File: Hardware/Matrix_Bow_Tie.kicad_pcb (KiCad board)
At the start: 2 copper layers, 17.8 x 13 mm, 2 parts, among them U1 MAX4466

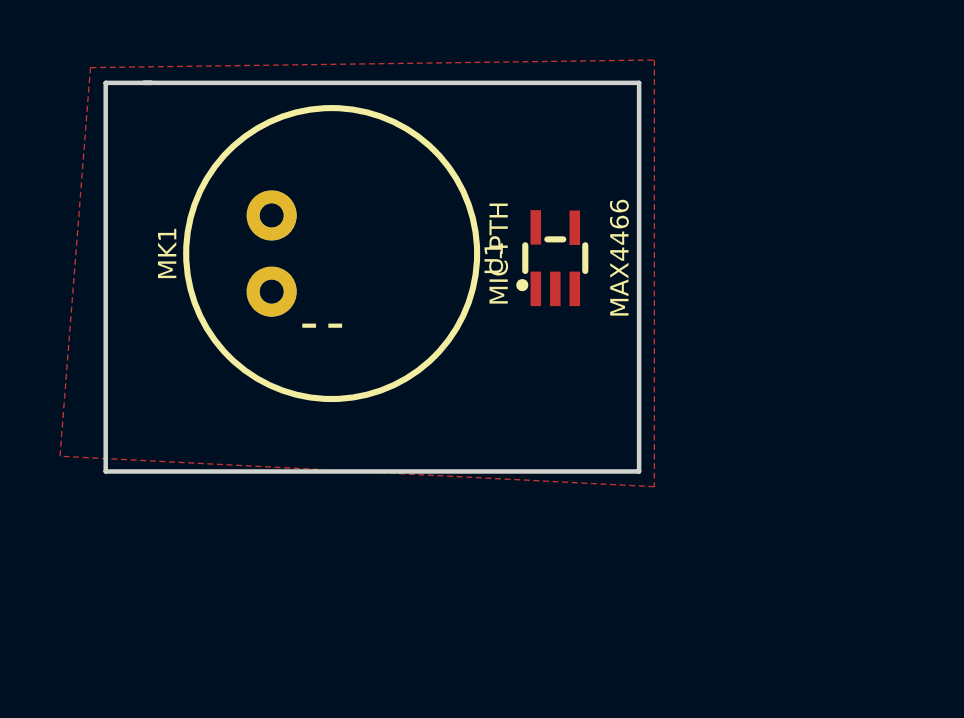
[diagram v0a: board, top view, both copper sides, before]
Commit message: Added trimpot footprint and drew mic amp circuit.
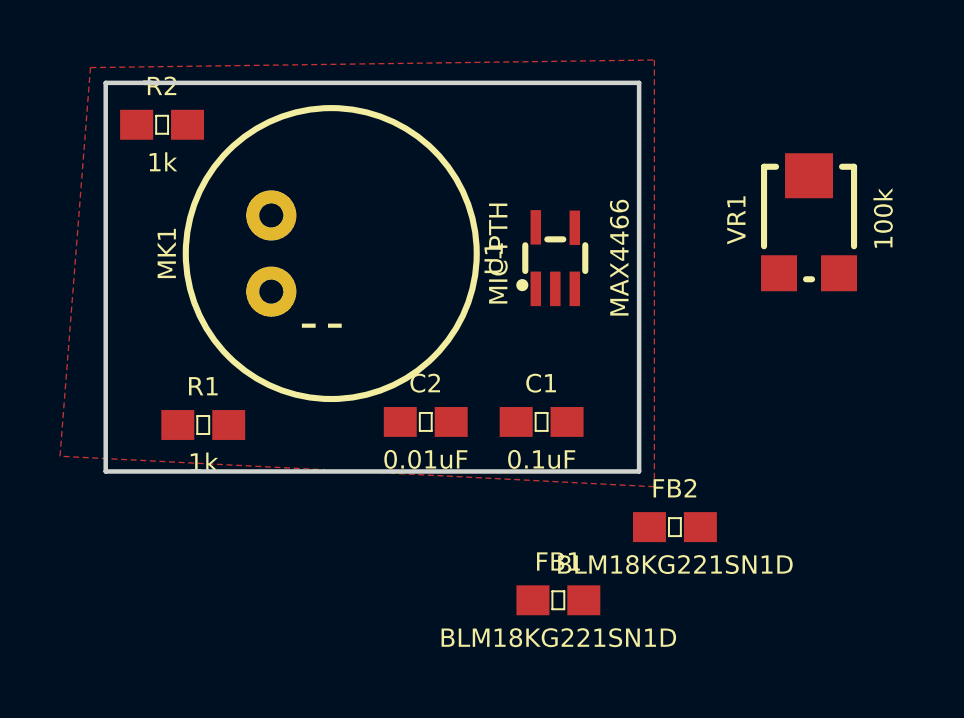
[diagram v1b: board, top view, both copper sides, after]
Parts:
- added C1: 0.1uF, 0603, F.Cu at (155.5, 110.6)
- added C2: 0.01uF, 0603, F.Cu at (151.6, 110.6)
- added FB1: BLM18KG221SN1D, 0603, F.Cu at (156.1, 116.6)
- added FB2: BLM18KG221SN1D, 0603, F.Cu at (159.9, 114.1)
- added R1: 1k, 0603, F.Cu at (144.2, 110.7)
- added R2: 1k, 0603, F.Cu at (142.8, 100.7)
- added VR1: 100k, TC33X, F.Cu at (164.4, 103.9)
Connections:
- net GND renamed AGND
- MK1 pad OUT: Net-(MK1-PadOUT) -> Net-(C2-Pad1)
- U1 pad 1: Net-(MK1-PadOUT) -> Net-(U1-Pad1)

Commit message: Parts mostly laid out
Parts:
- added C3: 10uF, Capacitors:0805, F.Cu at (181.6, 70.5)
- added C4: 100pF, Capacitors:0603, F.Cu at (186.7, 76.8)
- added C5: 0.1uF, Capacitors:0603, F.Cu at (212.1, 120.0)
- added D1: Yellow, LED:LED-0603, B.Cu at (209.5, 102.2)
- added D10: Yellow, LED:LED-0603, B.Cu at (198.1, 135.2)
- added D11: Yellow, LED:LED-0603, B.Cu at (186.7, 109.8)
- added D12: Yellow, LED:LED-0603, B.Cu at (187.9, 114.9)
- added D13: Yellow, LED:LED-0603, B.Cu at (188.6, 120.0)
- added D14: Yellow, LED:LED-0603, B.Cu at (187.9, 125.1)
- added D15: Yellow, LED:LED-0603, B.Cu at (186.7, 130.2)
- added D16: Yellow, LED:LED-0603, B.Cu at (175.2, 114.9)
- added D17: Yellow, LED:LED-0603, B.Cu at (175.9, 117.5)
- added D18: Yellow, LED:LED-0603, B.Cu at (175.9, 120.0)
- added D19: Yellow, LED:LED-0603, B.Cu at (175.9, 122.5)
- added D2: Yellow, LED:LED-0603, B.Cu at (210.8, 111.1)
- added D20: Yellow, LED:LED-0603, B.Cu at (175.2, 125.1)
- added D21: Yellow, LED:LED-0603, B.Cu at (144.8, 114.9)
- added D22: Yellow, LED:LED-0603, B.Cu at (144.1, 117.5)
- added D23: Yellow, LED:LED-0603, B.Cu at (144.1, 120.0)
- added D24: Yellow, LED:LED-0603, B.Cu at (144.1, 122.5)
- added D25: Yellow, LED:LED-0603, B.Cu at (144.8, 125.1)
- added D26: Yellow, LED:LED-0603, B.Cu at (133.3, 109.8)
- added D27: Yellow, LED:LED-0603, B.Cu at (132.1, 114.9)
- added D28: Yellow, LED:LED-0603, B.Cu at (131.4, 120.0)
- added D29: Yellow, LED:LED-0603, B.Cu at (132.1, 125.1)
- added D3: Yellow, LED:LED-0603, B.Cu at (211.4, 120.0)
- added D30: Yellow, LED:LED-0603, B.Cu at (133.3, 130.2)
- added D31: Yellow, LED:LED-0603, B.Cu at (121.9, 104.8)
- added D32: Yellow, LED:LED-0603, B.Cu at (120.6, 112.4)
- added D33: Yellow, LED:LED-0603, B.Cu at (120.0, 120.0)
- added D34: Yellow, LED:LED-0603, B.Cu at (120.6, 127.6)
- added D35: Yellow, LED:LED-0603, B.Cu at (121.9, 135.2)
- added D36: Yellow, LED:LED-0603, B.Cu at (110.5, 102.2)
- added D37: Yellow, LED:LED-0603, B.Cu at (109.2, 111.1)
- added D38: Yellow, LED:LED-0603, B.Cu at (108.6, 120.0)
- added D39: Yellow, LED:LED-0603, B.Cu at (109.2, 128.9)
- added D4: Yellow, LED:LED-0603, B.Cu at (210.8, 128.9)
- added D40: Yellow, LED:LED-0603, B.Cu at (110.5, 137.8)
- added D5: Yellow, LED:LED-0603, B.Cu at (209.5, 137.8)
- added D6: Yellow, LED:LED-0603, B.Cu at (198.1, 104.8)
- added D7: Yellow, LED:LED-0603, B.Cu at (199.4, 112.4)
- added D8: Yellow, LED:LED-0603, B.Cu at (200.0, 120.0)
- added D9: Yellow, LED:LED-0603, B.Cu at (199.4, 127.6)
- added H1: STAND-OFF, STAND-OFF, F.Cu at (150.5, 120.0)
- added H2: STAND-OFF, STAND-OFF, F.Cu at (169.5, 120.0)
- added J1: CONN_12, Matrix_Bot_Tie:1X12_SMD_MALE, F.Cu at (114.3, 128.9)
- added J2: CONN_12, Matrix_Bot_Tie:1X12_SMD_MALE, F.Cu at (114.3, 111.1)
- added Q1: TRANS_NPN_DUAL-MBT3904DW1T1, Silicon-Standard:SC70-6, F.Cu at (203.2, 132.7)
- added Q2: TRANS_NPN_DUAL-MBT3904DW1T1, Silicon-Standard:SC70-6, F.Cu at (208.3, 132.7)
- added Q3: TRANS_NPN_DUAL-MBT3904DW1T1, Silicon-Standard:SC70-6, F.Cu at (208.3, 107.3)
- added Q4: TRANS_NPN_DUAL-MBT3904DW1T1, Silicon-Standard:SC70-6, F.Cu at (203.2, 107.3)
- added R10: 470, Resistors:0603, F.Cu at (207.0, 127.6)
- added R11: 470, Resistors:0603, F.Cu at (209.5, 127.6)
- added R12: 470, Resistors:0603, F.Cu at (201.9, 127.6)
- added R13: 470, Resistors:0603, F.Cu at (209.5, 112.4)
- added R14: 470, Resistors:0603, F.Cu at (201.9, 112.4)
- added R15: 470, Resistors:0603, F.Cu at (207.0, 112.4)
- added R16: 470, Resistors:0603, F.Cu at (204.4, 112.4)
- added R17: 51, Resistors:0603, F.Cu at (109.2, 128.3)
- added R18: 51, Resistors:0603, F.Cu at (109.2, 124.5)
- added R19: 51, Resistors:0603, F.Cu at (109.2, 120.7)
- added R20: 51, Resistors:0603, F.Cu at (109.2, 116.8)
- added R21: 51, Resistors:0603, F.Cu at (109.2, 113.0)
- added R3: 1M, Resistors:0603, F.Cu at (180.3, 81.9)
- added R4: 1k, Resistors:0603, F.Cu at (185.4, 71.7)
- added R5: 1M, Resistors:0603, F.Cu at (181.6, 79.4)
- added R6: 22k, Resistors:0603, F.Cu at (186.7, 79.4)
- added R7: 10K, Resistors:0603, F.Cu at (115.5, 103.5)
- added R8: 10K, Resistors:0603, F.Cu at (199.4, 112.4)
- added R9: 470, Resistors:0603, F.Cu at (204.4, 127.6)
- added S1: MOMENTARY-SWITCH-SPST-2-SMD-4.6X2.8MM, Switches:TACTILE_SWITCH_SMD_4.6X2.8MM, F.Cu at (109.2, 103.5)
- added U2: 74HC4051-SOIC16, Matrix_Bot_Tie:SOIC-16, F.Cu at (205.7, 120.0)
- C1, C2: footprint 0603 -> Capacitors:0603
- FB1, FB2: footprint 0603 -> Coils:0603
- MK1: footprint MICROPHONE-PTH-9.7MM -> Silicon-Custom:MICROPHONE-PTH-9.7MM; moved to B.Cu
- R1, R2: footprint 0603 -> Resistors:0603
- VR1: footprint TC33X -> Matrix_Bot_Tie:TC33X
- moved FB1 50.6 mm to (174.0, 69.2), turned to 180 degrees
- moved FB2 43.4 mm to (174.0, 73.0), turned to 180 degrees
- moved R1 41.4 mm to (174.0, 81.9), turned to 180 degrees
- moved C2 40.5 mm to (174.0, 76.8)
- moved R2 37.7 mm to (174.0, 79.4), turned to 180 degrees
- moved U1 37.4 mm to (180.3, 76.8)
- moved C1 36.1 mm to (180.3, 84.4)
- moved VR1 29.5 mm to (186.7, 84.4)
- moved MK1 18.9 mm to (160.0, 120.0), turned to 270 degrees
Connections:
- U1 pad 1: Net-(U1-Pad1) -> Net-(C2-Pad2)
- U1 pad 4: Net-(U1-Pad4) -> OUT
- U1 pad 5: Net-(U1-Pad5) -> VCCA
- VR1 pad 1: Net-(U1-Pad4) -> OUT
- VR1 pad 2: Net-(VR1-Pad2) -> OUT
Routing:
- net E: track 0.00 -> 117.0 mm, vias 0 -> 2
- net Net-(D10-PadA): track 0.00 -> 113.5 mm
- net Net-(D1-PadA): track 0.00 -> 113.5 mm
- net Z: track 0.00 -> 111.0 mm, vias 0 -> 2
- net 3.3V: track 0.00 -> 100.6 mm
- net S1: track 0.00 -> 99.7 mm
- net S0: track 0.00 -> 98.4 mm
- net S2: track 0.00 -> 97.1 mm
- net OUT: track 0.00 -> 54.1 mm
- net Net-(D36-PadC): track 0.00 -> 37.1 mm
- net Net-(D1-PadC): track 0.00 -> 37.1 mm
- net Net-(D13-PadA): track 0.00 -> 34.6 mm
- net Net-(D14-PadA): track 0.00 -> 32.9 mm
- net Net-(D12-PadA): track 0.00 -> 32.5 mm
- net Net-(D31-PadC): track 0.00 -> 32.1 mm
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- removed copper zone on F.Cu, net AGND
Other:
- board size 17.8 x 13 mm -> 116.8 x 55.9 mm
- net class Default: clearance 0.254 -> 0.2032; via_dia 0.6 -> 1.016; via_drill 0.4 -> 0.508
- net class Power added: clearance 0.2032, trace_width 0.508, via_dia 1.016, via_drill 0.508
- rule trace_clearance: 0.254 -> 0.2032

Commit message: Added BOM
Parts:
- moved C3 56.2 mm to (187.9, 126.3), turned to 90 degrees
- moved R4 54.6 mm to (185.4, 126.3), turned to 90 degrees
- moved C4 51.1 mm to (181.6, 127.6)
- moved R1 47.9 mm to (191.8, 126.3), turned to 0 degrees
- moved R2 44.9 mm to (193.0, 120.0), turned to 90 degrees
- moved FB1 43.8 mm to (181.6, 112.4)
- moved U1 43.6 mm to (186.7, 120.0), turned to 180 degrees
- moved FB2 42.6 mm to (181.6, 114.9)
- moved C2 40.4 mm to (190.5, 113.7), turned to 90 degrees
- moved VR1 38.4 mm to (181.6, 122.5), turned to 180 degrees
- moved R6 38.4 mm to (181.6, 117.5), turned to 180 degrees
- moved C1 37.0 mm to (190.5, 120.0), turned to 90 degrees
- moved R5 35.9 mm to (186.7, 114.9), turned to 180 degrees
- moved R3 31.1 mm to (186.7, 112.4), turned to 0 degrees
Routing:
- net Net-(C2-Pad1): track 24.0 -> 63.5 mm
- net VCCA: track 0.00 -> 26.7 mm, vias 0 -> 2
- net OUT: track 54.1 -> 79.4 mm
- net AGND: track 0.00 -> 21.8 mm, vias 0 -> 6
- net Net-(C4-Pad2): track 0.00 -> 16.8 mm
- net Net-(C2-Pad2): track 0.00 -> 9.81 mm
- net Net-(C1-Pad1): track 0.00 -> 8.22 mm
- net 3.3V: track 100.6 -> 106.5 mm
- net GND: track 0.00 -> 4.00 mm, vias 0 -> 1
- net Net-(R6-Pad2): track 0.00 -> 3.34 mm
- net Net-(C3-Pad1): track 0.00 -> 2.56 mm
- net S0: track 98.4 -> 100.1 mm
- net S1: track 99.7 -> 101.2 mm
- net S2: track 97.1 -> 98.5 mm
- net E: track 117.0 -> 118.2 mm
- added copper zone on B.Cu, net AGND
- added copper zone on F.Cu, net AGND

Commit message: More progress on layout
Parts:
- moved R17 13.4 mm to (109.2, 114.9), turned to 180 degrees
- moved S1 12.8 mm to (121.9, 104.8)
- moved R18 7.00 mm to (109.2, 117.5), turned to 180 degrees
- moved R21 6.97 mm to (109.2, 120.0)
- moved R20 5.70 mm to (109.2, 122.5)
- moved R19 4.43 mm to (109.2, 125.1)
- moved R7 1.80 mm to (116.8, 104.8), turned to 90 degrees
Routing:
- net Net-(D26-PadC): track 21.9 -> 148.2 mm, vias 0 -> 3
- net Net-(D21-PadC): track 10.7 -> 131.3 mm, vias 0 -> 3
- net Net-(D36-PadC): track 37.1 -> 144.9 mm, vias 0 -> 1
- net Net-(D31-PadC): track 32.1 -> 119.8 mm, vias 0 -> 3
- net Net-(D12-PadA): track 32.5 -> 115.9 mm, vias 0 -> 1
- net Net-(D14-PadA): track 32.9 -> 108.7 mm, vias 0 -> 1
- net R2: track 0.00 -> 60.7 mm
- net R3: track 0.00 -> 53.8 mm
- net Net-(D13-PadA): track 34.6 -> 88.2 mm, vias 0 -> 6
- net R4: track 0.00 -> 47.2 mm
- net 3.3V: track 106.5 -> 146.1 mm
- net R0: track 0.00 -> 30.9 mm
- net R1: track 0.00 -> 27.3 mm
- net Net-(D10-PadA): track 113.5 -> 135.5 mm, vias 0 -> 1
- net Net-(Q3-Pad2): track 0.00 -> 21.7 mm
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
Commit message: Layout complete. Gerbers ran.
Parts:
- added LOGO1: OSHW-LOGOS, OSHW-LOGO-S, F.Cu at (209.1, 137.1)
- moved R1 3.17 mm to (191.8, 123.2)
- moved C4 2.01 mm to (182.2, 125.7)
- moved FB1 2.01 mm to (182.2, 114.3)
- moved R3 1.91 mm to (186.7, 114.3)
- moved FB2 1.42 mm to (182.2, 116.2)
- moved C2 1.27 mm to (190.5, 114.9)
- moved C3 1.27 mm to (187.9, 125.1)
- moved R4 1.27 mm to (185.4, 125.1)
- moved R5 1.27 mm to (186.7, 116.2)
- moved R6 0.90 mm to (182.2, 118.1)
- moved VR1 0.90 mm to (182.2, 121.9)
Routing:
- net GND: track 4.07 -> 551.7 mm, vias 1 -> 60
- net Net-(D12-PadA): track 115.9 -> 184.3 mm, vias 1 -> 3
- net Net-(D14-PadA): track 108.7 -> 173.0 mm
- net Net-(D13-PadA): track 88.2 -> 149.2 mm, vias 6 -> 10
- net Net-(D16-PadC): track 10.7 -> 52.9 mm, vias 0 -> 3
- net Net-(D11-PadC): track 21.9 -> 46.5 mm, vias 0 -> 1
- net AGND: track 21.8 -> 46.0 mm, vias 6 -> 8
- net Z: track 112.8 -> 125.5 mm
- net Net-(D1-PadA): track 131.9 -> 143.9 mm
- net Net-(D1-PadC): track 37.1 -> 46.9 mm, vias 0 -> 1
- net 3.3V: track 146.1 -> 154.0 mm
- net VCCA: track 26.7 -> 19.0 mm
- net Net-(D10-PadC): track 33.4 -> 40.7 mm, vias 0 -> 1
- net Net-(C1-Pad1): track 8.22 -> 5.22 mm
- net Net-(C4-Pad2): track 16.8 -> 14.6 mm
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- added copper zone on B.Cu, net GND
- added copper zone on F.Cu, net GND
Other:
- outline, holes or cut-outs redrawn
- board text added: "Matrix Bow Tie"
- board text added: "v01"

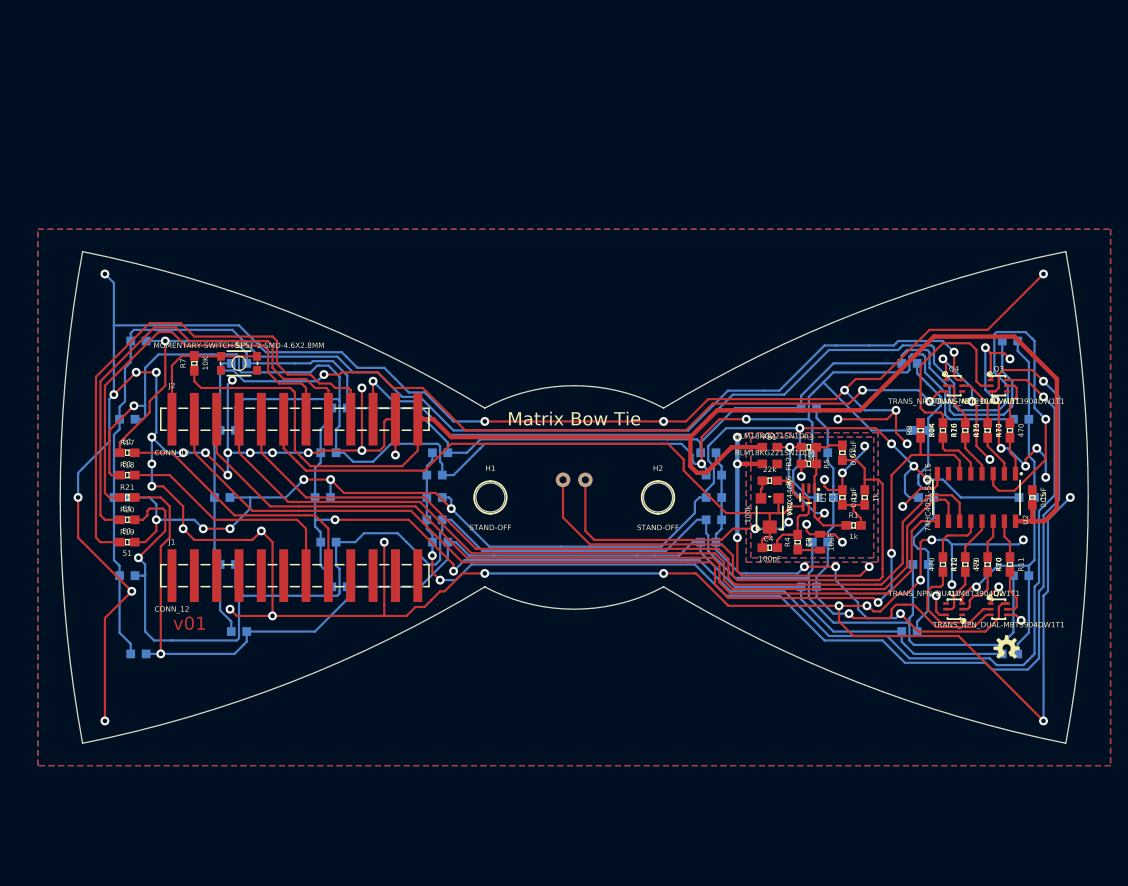
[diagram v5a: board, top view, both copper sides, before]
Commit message: Re-did copper pour. Magic happened. It fits the outline better now.
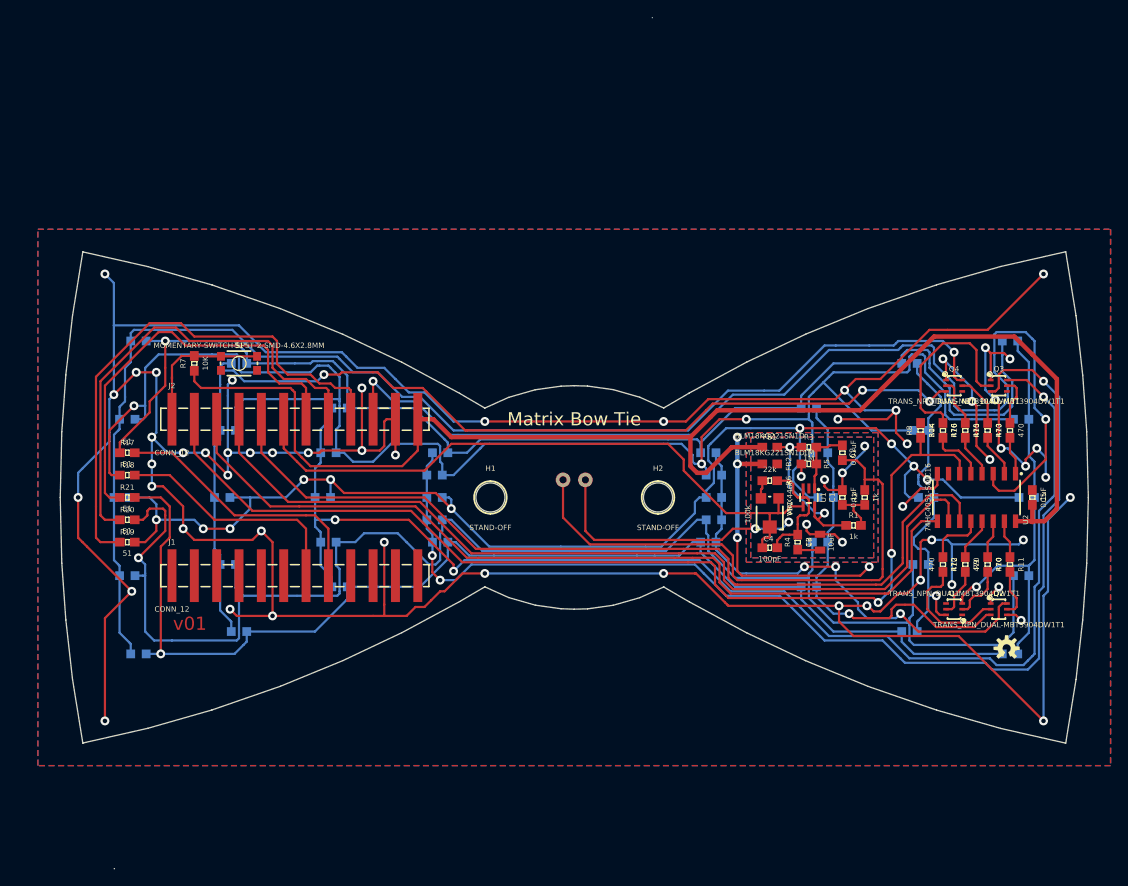
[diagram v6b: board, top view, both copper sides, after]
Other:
- board size 116.8 x 55.9 mm -> 116.9 x 96.7 mm
